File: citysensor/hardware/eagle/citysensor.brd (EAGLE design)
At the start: 65.7 x 31.7 mm, 25 parts, among them U1 ATMEGA328P_TQFP, X1 16MHZ

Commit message: hooked up reset pin
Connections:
- net PIRESET: now also U$1.P$11
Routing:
- net PIRESET: track 0.00 -> 9.59 mm, vias 0 -> 1
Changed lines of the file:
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@@
 <grid distance="50" unitdist="mil" unit="mil" style="lines" multiple="1" display="no" altdistance="5" altunitdist="mil" altunit="mil"/>
 <layers>
-<layer number="1" name="Top" color="4" fill="1" visible="no" active="yes"/>
-<layer number="16" name="Bottom" color="1" fill="1" visible="yes" active="yes"/>
+<layer number="1" name="Top" color="4" fill="1" visible="yes" active="yes"/>
+<layer number="16" name="Bottom" color="1" fill="1" visible="no" active="yes"/>
 <layer number="17" name="Pads" color="2" fill="1" visible="yes" active="yes"/>
 <layer number="18" name="Vias" color="2" fill="1" visible="yes" active="yes"/>
 <layer number="19" name="Unrouted" color="6" fill="1" visible="yes" active="yes"/>
 <layer number="20" name="Dimension" color="24" fill="1" visible="yes" active="yes"/>
-<layer number="21" name="tPlace" color="7" fill="1" visible="no" active="yes"/>
-<layer number="22" name="bPlace" color="7" fill="1" visible="yes" active="yes"/>
-<layer number="23" name="tOrigins" color="15" fill="1" visible="no" active="yes"/>
-<layer number="24" name="bOrigins" color="15" fill="1" visible="yes" active="yes"/>
-<layer number="25" name="tNames" color="7" fill="1" visible="no" active="yes"/>
-<layer number="26" name="bNames" color="7" fill="1" visible="yes" active="yes"/>
+<layer number="21" name="tPlace" color="7" fill="1" visible="yes" active="yes"/>
+<layer number="22" name="bPlace" color="7" fill="1" visible="no" active="yes"/>
+<layer number="23" name="tOrigins" color="15" fill="1" visible="yes" active="yes"/>
+<layer number="24" name="bOrigins" color="15" fill="1" visible="no" active="yes"/>
+<layer number="25" name="tNames" color="7" fill="1" visible="yes" active="yes"/>
+<layer number="26" name="bNames" color="7" fill="1" visible="no" active="yes"/>
 <layer number="27" name="tValues" color="7" fill="1" visible="no" active="yes"/>
 <layer number="28" name="bValues" color="7" fill="1" visible="no" active="yes"/>
@@
 <layer number="37" name="tTest" color="7" fill="1" visible="no" active="yes"/>
 <layer number="38" name="bTest" color="7" fill="1" visible="no" active="yes"/>
-<layer number="39" name="tKeepout" color="4" fill="11" visible="no" active="yes"/>
-<layer number="40" name="bKeepout" color="1" fill="11" visible="yes" active="yes"/>
-<layer number="41" name="tRestrict" color="4" fill="10" visible="no" active="yes"/>
-<layer number="42" name="bRestrict" color="1" fill="10" visible="yes" active="yes"/>
+<layer number="39" name="tKeepout" color="4" fill="11" visible="yes" active="yes"/>
+<layer number="40" name="bKeepout" color="1" fill="11" visible="no" active="yes"/>
+<layer number="41" name="tRestrict" color="4" fill="10" visible="yes" active="yes"/>
+<layer number="42" name="bRestrict" color="1" fill="10" visible="no" active="yes"/>
 <layer number="43" name="vRestrict" color="2" fill="10" visible="no" active="yes"/>
 <layer number="44" name="Drills" color="7" fill="1" visible="no" active="yes"/>
@@
 <layer number="49" name="Reference" color="7" fill="1" visible="no" active="yes"/>
 <layer number="50" name="dxf" color="7" fill="1" visible="no" active="no"/>
-<layer number="51" name="tDocu" color="7" fill="1" visible="no" active="yes"/>
-<layer number="52" name="bDocu" color="7" fill="1" visible="yes" active="yes"/>
+<layer number="51" name="tDocu" color="7" fill="1" visible="yes" active="yes"/>
+<layer number="52" name="bDocu" color="7" fill="1" visible="no" active="yes"/>
 <layer number="53" name="tGND_GNDA" color="7" fill="9" visible="no" active="no"/>
 <layer number="54" name="bGND_GNDA" color="1" fill="9" visible="no" active="no"/>
@@
 <signal name="PIRESET">
 <contactref element="C6" pad="2"/>
+<via x="17.526" y="21.717" extent="1-16" drill="0.35"/>
+<wire x1="19.177" y1="22.54" x2="18.095" y2="22.032" width="0.3048" layer="1"/>
+<wire x1="18.095" y1="22.032" x2="17.526" y2="21.717" width="0.3048" layer="1"/>
+<contactref element="U$1" pad="P$11"/>
+<wire x1="17.526" y1="21.717" x2="21.59" y2="21.717" width="0.3048" layer="16"/>
+<wire x1="21.59" y1="21.717" x2="21.59" y2="25.4" width="0.3048" layer="16"/>
 </signal>
 <signal name="VCC">

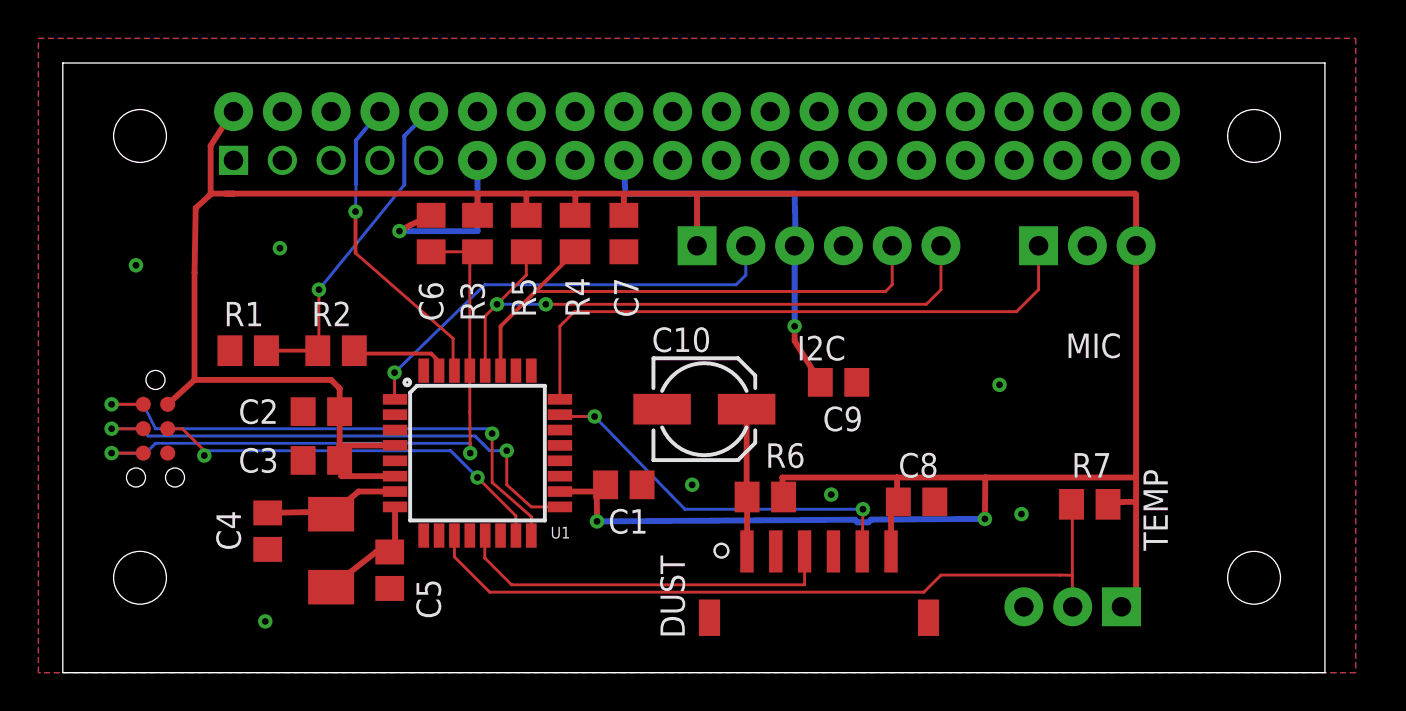
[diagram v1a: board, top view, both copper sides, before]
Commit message: added switch locations to eagle file
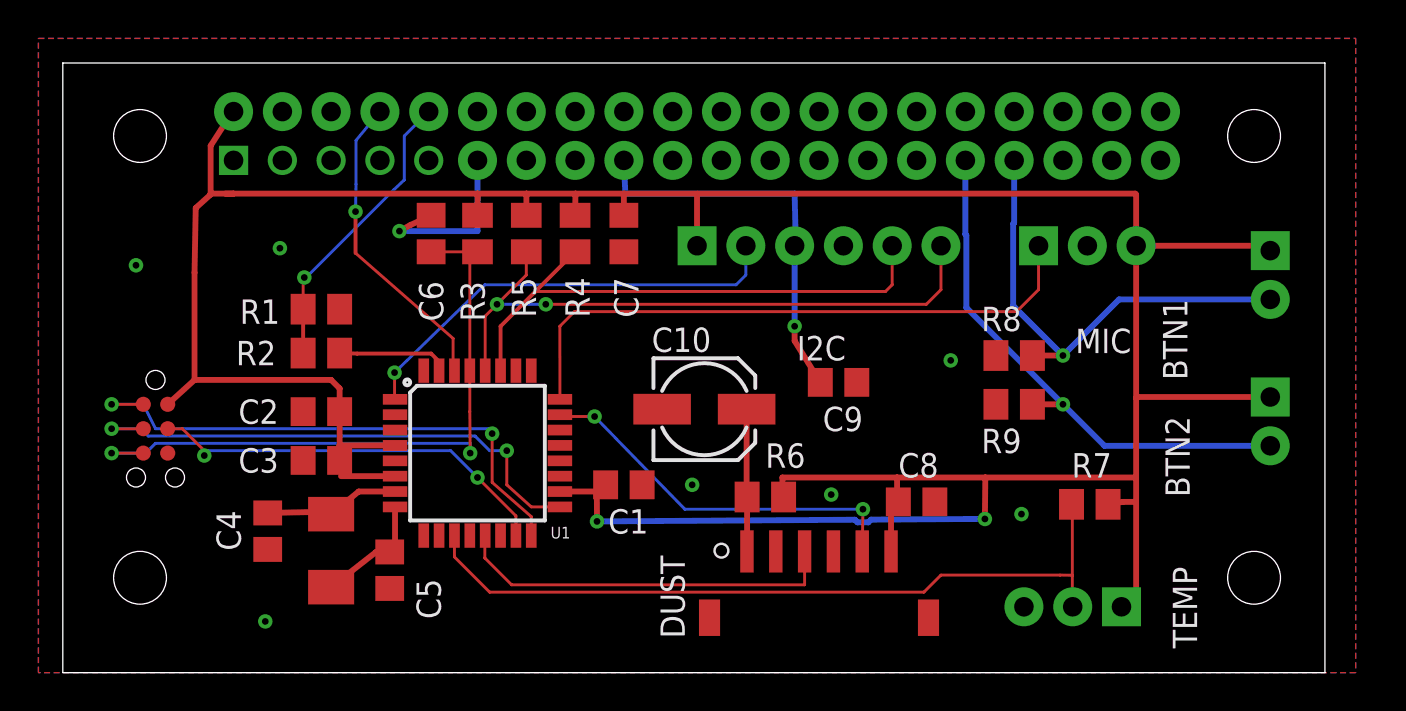
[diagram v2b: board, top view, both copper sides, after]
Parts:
- added BTN1, BTN2: BTN, citysensor:MOLEX_2
- added R8, R9: 10k, resistor:M0805
- moved R1 4.38 mm to (13.5, 17.7), turned to 180 degrees
- moved R2 0.77 mm to (13.5, 15.4)
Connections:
- new net BTN1OUT: BTN1.P$2, R8.1, U$1.P$33
- new net BTN2OUT: BTN2.P$2, R9.1, U$1.P$31
- net GND: now also R8.2, R9.2
- net VCC: now also BTN1.P$1, BTN2.P$1
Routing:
- net BTN2OUT: track 0.00 -> 28.1 mm, vias 0 -> 1
- net BTN1OUT: track 0.00 -> 24.8 mm, vias 0 -> 1
- net VCC: track 165.9 -> 180.0 mm
- net PIRX: track 17.2 -> 15.3 mm
- net ARDTX: track 5.12 -> 5.82 mm
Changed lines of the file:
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@@
 <attribute name="NAME" x="19.812" y="17.018" size="1.27" layer="25" rot="R90"/>
 </element>
-<element name="R1" library="resistor" library_urn="urn:adsk.eagle:library:348" package="M0805" package3d_urn="urn:adsk.eagle:package:26079/1" value="1k" x="9.652" y="15.494" smashed="yes">
-<attribute name="NAME" x="8.382" y="16.764" size="1.27" layer="25"/>
-</element>
-<element name="R2" library="resistor" library_urn="urn:adsk.eagle:library:348" package="M0805" package3d_urn="urn:adsk.eagle:package:26079/1" value="510" x="14.224" y="15.494" smashed="yes">
-<attribute name="NAME" x="12.954" y="16.764" size="1.27" layer="25"/>
+<element name="R1" library="resistor" library_urn="urn:adsk.eagle:library:348" package="M0805" package3d_urn="urn:adsk.eagle:package:26079/1" value="1k" x="13.462" y="17.653" smashed="yes" rot="R180">
+<attribute name="NAME" x="11.303" y="18.161" size="1.27" layer="25" rot="R180"/>
+</element>
+<element name="R2" library="resistor" library_urn="urn:adsk.eagle:library:348" package="M0805" package3d_urn="urn:adsk.eagle:package:26079/1" value="510" x="13.462" y="15.367" smashed="yes">
+<attribute name="NAME" x="9.017" y="14.732" size="1.27" layer="25"/>
 </element>
 <element name="R3" library="resistor" library_urn="urn:adsk.eagle:library:348" package="M0805" package3d_urn="urn:adsk.eagle:package:26079/1" value="10k" x="21.59" y="21.59" smashed="yes" rot="R90">
@@
 </element>
 <element name="TEMP" library="citysensor" package="MOLEX_3" value="DHT11" x="52.578" y="2.159" smashed="yes">
-<attribute name="NAME" x="57.531" y="5.08" size="1.27" layer="21" rot="R90"/>
+<attribute name="NAME" x="59.055" y="0" size="1.27" layer="21" rot="R90"/>
 </element>
 <element name="DUST" library="citysensor" package="S6B-ZR-SM4A-TF" value="GP2Y1010AU0F" x="39.37" y="2.54" smashed="yes" rot="R180">
@@
 </element>
 <element name="MIC" library="citysensor" package="MOLEX_3" value="MIC" x="53.34" y="20.955" smashed="yes" rot="R180">
-<attribute name="NAME" x="55.118" y="16.383" size="1.27" layer="21" rot="R180"/>
+<attribute name="NAME" x="55.626" y="16.637" size="1.27" layer="21" rot="R180"/>
 </element>
 <element name="C7" library="resistor" library_urn="urn:adsk.eagle:library:348" package="C0805" package3d_urn="urn:adsk.eagle:package:26137/1" value=".1uF" x="29.21" y="21.59" smashed="yes" rot="R270">
@@
 <element name="R7" library="resistor" library_urn="urn:adsk.eagle:library:348" package="M0805" package3d_urn="urn:adsk.eagle:package:26079/1" value="10k" x="53.467" y="7.493" smashed="yes" rot="R180">
 <attribute name="NAME" x="54.61" y="10.16" size="1.27" layer="25" rot="R180"/>
+</element>
+<element name="BTN1" library="citysensor" package="MOLEX_2" value="BTN" x="62.865" y="19.431" smashed="yes" rot="R90">
+<attribute name="NAME" x="58.547" y="13.97" size="1.27" layer="21" rot="R90"/>
+</element>
+<element name="BTN2" library="citysensor" package="MOLEX_2" value="BTN" x="62.865" y="11.811" smashed="yes" rot="R90">
+<attribute name="NAME" x="58.674" y="7.874" size="1.27" layer="21" rot="R90"/>
+</element>
+<element name="R8" library="resistor" library_urn="urn:adsk.eagle:library:348" package="M0805" package3d_urn="urn:adsk.eagle:package:26079/1" value="10k" x="49.53" y="15.24" smashed="yes" rot="R180">
+<attribute name="NAME" x="49.911" y="17.78" size="1.27" layer="25" rot="R180"/>
+<attribute name="VALUE" x="50.8" y="17.78" size="1.27" layer="27" rot="R180"/>
+</element>
+<element name="R9" library="resistor" library_urn="urn:adsk.eagle:library:348" package="M0805" package3d_urn="urn:adsk.eagle:package:26079/1" value="10k" x="49.53" y="12.7" smashed="yes" rot="R180">
+<attribute name="NAME" x="49.911" y="11.43" size="1.27" layer="25" rot="R180"/>
+<attribute name="VALUE" x="50.8" y="15.24" size="1.27" layer="27" rot="R180"/>
 </element>
 </elements>
@@
 <contactref element="U1" pad="5"/>
 <via x="32.766" y="8.509" extent="1-16" drill="0.35"/>
-<via x="48.768" y="13.716" extent="1-16" drill="0.35"/>
+<via x="46.228" y="14.986" extent="1-16" drill="0.35"/>
 <via x="49.911" y="6.985" extent="1-16" drill="0.35"/>
 <via x="40.005" y="8.001" extent="1-16" drill="0.35"/>
@@
 <vertex x="-1.27" y="-1.27"/>
 </polygon>
+<contactref element="R8" pad="2"/>
+<contactref element="R9" pad="2"/>
 </signal>
 <signal name="5V_2">
@@
 <contactref element="U1" pad="30"/>
 <via x="15.24" y="22.733" extent="1-16" drill="0.35"/>
-<wire x1="16.51" y1="27.94" x2="15.2654" y2="26.4414" width="0.2032" layer="16"/>
-<wire x1="15.2654" y1="26.4414" x2="15.2654" y2="24.16046875" width="0.2032" layer="16"/>
+<wire x1="16.51" y1="27.94" x2="15.2654" y2="26.4414" width="0.1524" layer="16"/>
+<wire x1="15.2654" y1="26.4414" x2="15.2654" y2="24.16046875" width="0.1524" layer="16"/>
 <wire x1="15.24" y1="22.733" x2="15.24" y2="20.574" width="0.2032" layer="1"/>
 <wire x1="20.39" y1="14.4526" x2="20.39" y2="14.9262125" width="0.2032" layer="1"/>
@@
 <contactref element="U1" pad="31"/>
 <contactref element="R2" pad="2"/>
-<wire x1="15.174" y1="15.494" x2="15.3264" y2="15.3416" width="0.2032" layer="1"/>
+<wire x1="14.412" y1="15.367" x2="15.3264" y2="15.3416" width="0.2032" layer="1"/>
 <wire x1="19.1746125" y1="15.3416" x2="19.59" y2="14.9262125" width="0.2032" layer="1"/>
 <wire x1="19.59" y1="14.9262125" x2="19.59" y2="14.4526" width="0.2032" layer="1"/>
@@
 <contactref element="R1" pad="2"/>
 <contactref element="R2" pad="1"/>
-<wire x1="13.274" y1="15.494" x2="10.602" y2="15.494" width="0.2032" layer="1"/>
-<via x="13.335" y="18.669" extent="1-16" drill="0.35"/>
-<wire x1="13.335" y1="15.555" x2="13.274" y2="15.494" width="0.2032" layer="1"/>
-<wire x1="19.05" y1="27.94" x2="17.78" y2="26.67" width="0.2032" layer="16"/>
-<wire x1="17.78" y1="26.67" x2="17.78" y2="24.13" width="0.2032" layer="16"/>
-<wire x1="17.78" y1="24.13" x2="13.335" y2="18.669" width="0.1524" layer="16"/>
-<wire x1="13.335" y1="18.669" x2="13.335" y2="15.555" width="0.1524" layer="1"/>
+<wire x1="12.512" y1="17.653" x2="12.512" y2="15.367" width="0.2032" layer="1"/>
+<via x="12.573" y="19.304" extent="1-16" drill="0.35"/>
+<wire x1="19.05" y1="27.94" x2="17.78" y2="26.67" width="0.1524" layer="16"/>
+<wire x1="17.78" y1="24.384" x2="17.78" y2="26.67" width="0.1524" layer="16"/>
+<wire x1="17.78" y1="24.384" x2="17.24115" y2="23.876" width="0.1524" layer="16"/>
+<wire x1="12.66915" y1="19.304" x2="12.573" y2="19.304" width="0.1524" layer="16"/>
+<wire x1="17.24115" y1="23.876" x2="12.66915" y2="19.304" width="0.1524" layer="16"/>
+<wire x1="12.573" y1="19.304" x2="12.512" y2="19.243" width="0.1524" layer="1"/>
+<wire x1="12.512" y1="19.243" x2="12.512" y2="17.653" width="0.1524" layer="1"/>
 </signal>
 <signal name="N$5">
@@
 <wire x1="55.832" y1="23.67" x2="55.88" y2="23.622" width="0.3048" layer="1"/>
 <wire x1="55.88" y1="23.622" x2="55.88" y2="20.955" width="0.3048" layer="1"/>
-<wire x1="55.88" y1="20.955" x2="55.88" y2="8.89" width="0.3048" layer="1"/>
+<wire x1="55.88" y1="13.02060625" x2="55.88" y2="20.955" width="0.3048" layer="1"/>
+<wire x1="55.88" y1="13.02060625" x2="55.88" y2="8.89" width="0.3048" layer="1"/>
 <wire x1="55.88" y1="8.89" x2="55.88" y2="7.62" width="0.3048" layer="1"/>
 <wire x1="55.88" y1="7.62" x2="55.88" y2="2.921" width="0.3048" layer="1"/>
@@
 <wire x1="48.006" y1="6.731" x2="48.029128125" y2="8.89" width="0.3048" layer="1"/>
 <wire x1="27.813" y1="6.604" x2="27.801765625" y2="8.16" width="0.3048" layer="1"/>
+<contactref element="BTN1" pad="P$1"/>
+<contactref element="BTN2" pad="P$1"/>
+<wire x1="55.88" y1="20.955" x2="62.611" y2="20.955" width="0.3048" layer="1"/>
+<wire x1="62.611" y1="20.955" x2="62.865" y2="20.701" width="0.3048" layer="1"/>
+<wire x1="62.865" y1="13.081" x2="55.94039375" y2="13.081" width="0.3048" layer="1"/>
+<wire x1="55.94039375" y1="13.081" x2="55.88" y2="13.02060625" width="0.3048" layer="1"/>
 </signal>
 <signal name="N$9">
@@
 <wire x1="41.656" y1="7.239" x2="41.62" y2="5.04" width="0.1524" layer="1"/>
 </signal>
+<signal name="BTN1OUT">
+<contactref element="R8" pad="1"/>
+<contactref element="BTN1" pad="P$2"/>
+<via x="52.07" y="15.24" extent="1-16" drill="0.35"/>
+<wire x1="62.865" y1="18.161" x2="54.991" y2="18.161" width="0.3048" layer="16"/>
+<wire x1="54.991" y1="18.161" x2="52.07" y2="15.24" width="0.3048" layer="16"/>
+<wire x1="52.07" y1="15.24" x2="50.48" y2="15.24" width="0.3048" layer="1"/>
+<contactref element="U$1" pad="P$33"/>
+<wire x1="49.4792" y1="22.09725" x2="49.53" y2="22.14805" width="0.3048" layer="16"/>
+<wire x1="49.53" y1="22.14805" x2="49.53" y2="25.4" width="0.3048" layer="16"/>
+<wire x1="52.07" y1="15.24" x2="49.4792" y2="17.8308" width="0.3048" layer="16"/>
+<wire x1="49.4792" y1="17.8308" x2="49.4792" y2="22.09725" width="0.3048" layer="16"/>
+</signal>
+<signal name="BTN2OUT">
+<contactref element="BTN2" pad="P$2"/>
+<contactref element="R9" pad="1"/>
+<via x="52.07" y="12.7" extent="1-16" drill="0.35"/>
+<wire x1="62.865" y1="10.541" x2="54.229" y2="10.541" width="0.3048" layer="16"/>
+<wire x1="54.229" y1="10.541" x2="52.07" y2="12.7" width="0.3048" layer="16"/>
+<wire x1="52.07" y1="12.7" x2="50.48" y2="12.7" width="0.3048" layer="1"/>
+<contactref element="U$1" pad="P$31"/>
+<wire x1="47.0408" y1="21.50209375" x2="46.99" y2="21.55289375" width="0.3048" layer="16"/>
+<wire x1="46.99" y1="21.55289375" x2="46.99" y2="25.4" width="0.3048" layer="16"/>
+<wire x1="52.07" y1="12.7" x2="47.0408" y2="17.7292" width="0.3048" layer="16"/>
+<wire x1="47.0408" y1="17.7292" x2="47.0408" y2="21.50209375" width="0.3048" layer="16"/>
+</signal>
 </signals>

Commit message: added an rgbled component to the city sensor lib. Added a normal led to the board for arduino status
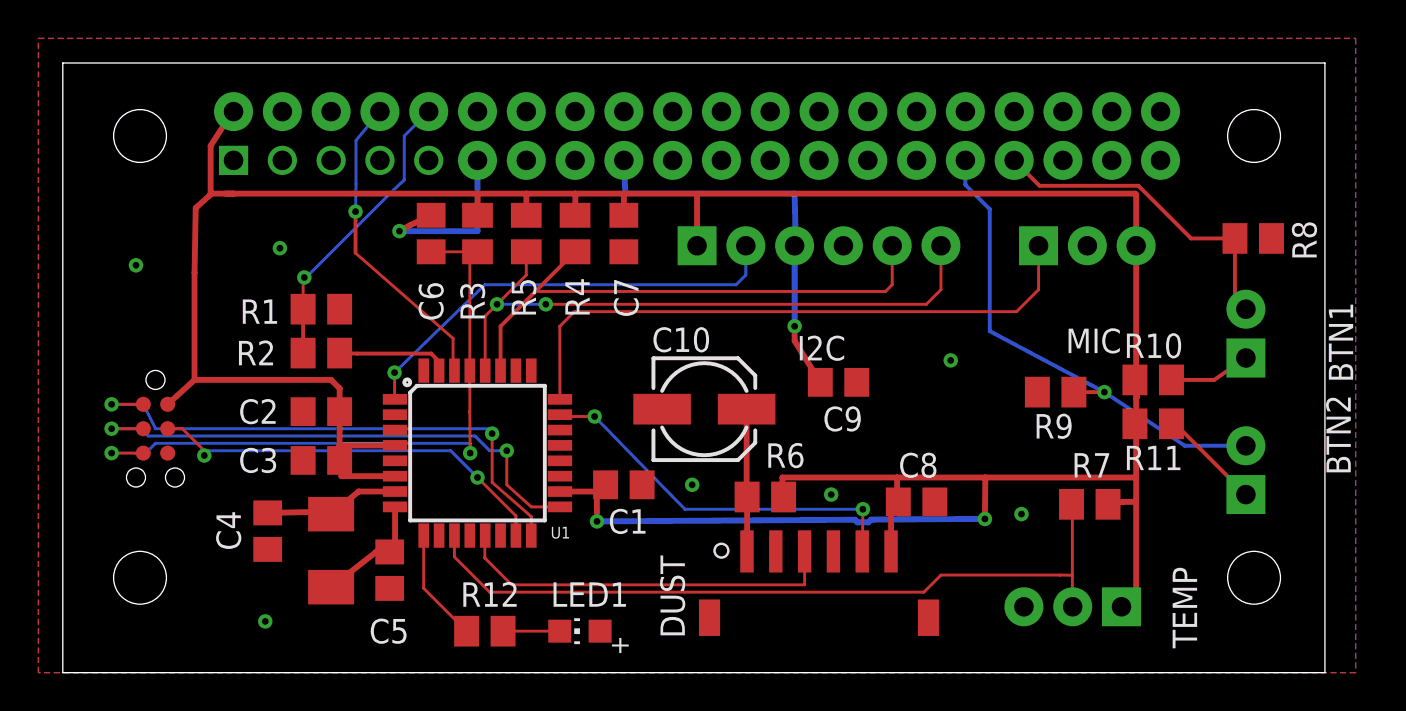
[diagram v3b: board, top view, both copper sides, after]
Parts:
- added LED1: (no value), adafruit:CHIP-LED0805
- added R10, R11: 1k, resistor:M0805
- added R12: 330, resistor:M0805
- moved R8 13.9 mm to (62.0, 21.3), turned to 0 degrees
- moved BTN1 3.30 mm to (61.6, 16.4), turned to 270 degrees
- moved BTN2 2.84 mm to (61.6, 9.27), turned to 270 degrees
- moved R9 2.25 mm to (51.7, 13.3)
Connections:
- new net N$1: BTN1.P$1, R10.2
- new net N$2: BTN2.P$1, R11.2
- new net N$3: R12.1, U1.9
- new net N$4: LED1.C, R12.2
- net GND: now also LED1.A
- net VCC: now also R10.1, R11.1; no longer BTN1.P$1, BTN2.P$1
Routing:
- net VCC: track 180.0 -> 166.2 mm
- net BTN1OUT: track 24.8 -> 17.1 mm, vias 1 -> 0
- net N$3: track 0.00 -> 5.90 mm
- net N$2: track 0.00 -> 5.40 mm
- net N$1: track 0.00 -> 4.23 mm
- net N$4: track 0.00 -> 2.95 mm
- net BTN2OUT: track 28.1 -> 26.0 mm
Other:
- board text added: "X1"
